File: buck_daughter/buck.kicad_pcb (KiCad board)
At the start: 2 copper layers, 35.6 x 15.2 mm, 21 parts, among them P1 Modular Jack In, U1 LD1117, U2 AP73333, U3 ST485E, U4 TPS54360DDAR

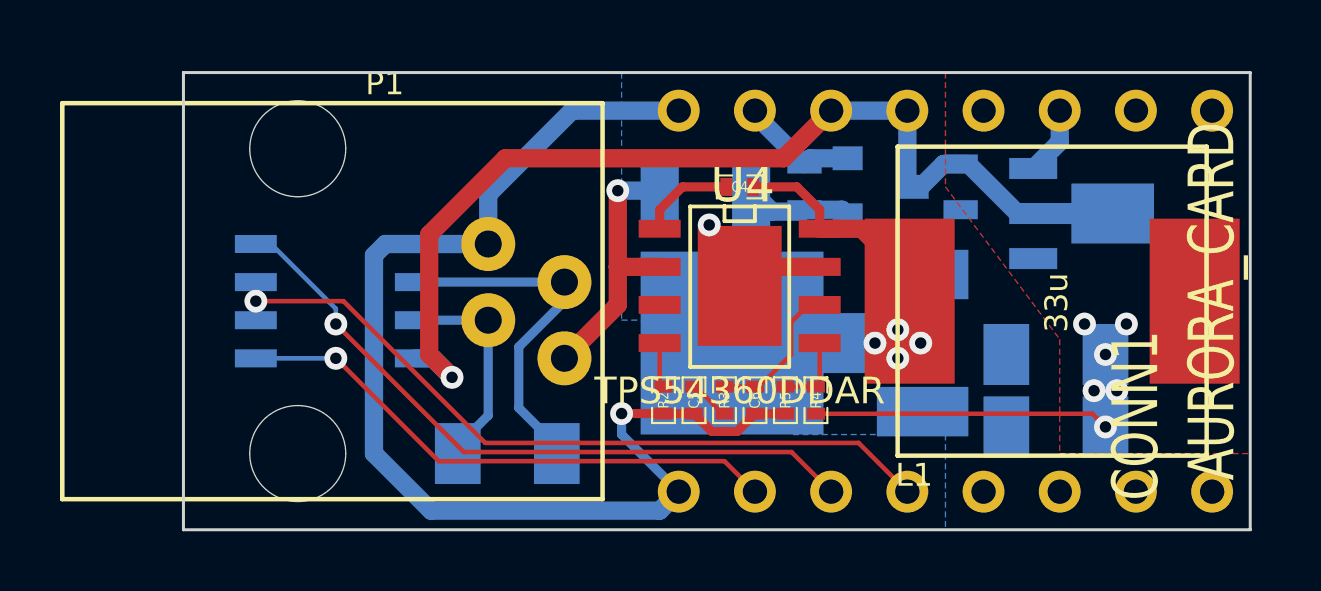
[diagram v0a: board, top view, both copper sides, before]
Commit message: Finished silkscreen on daughter board, it and digital led board are done\!
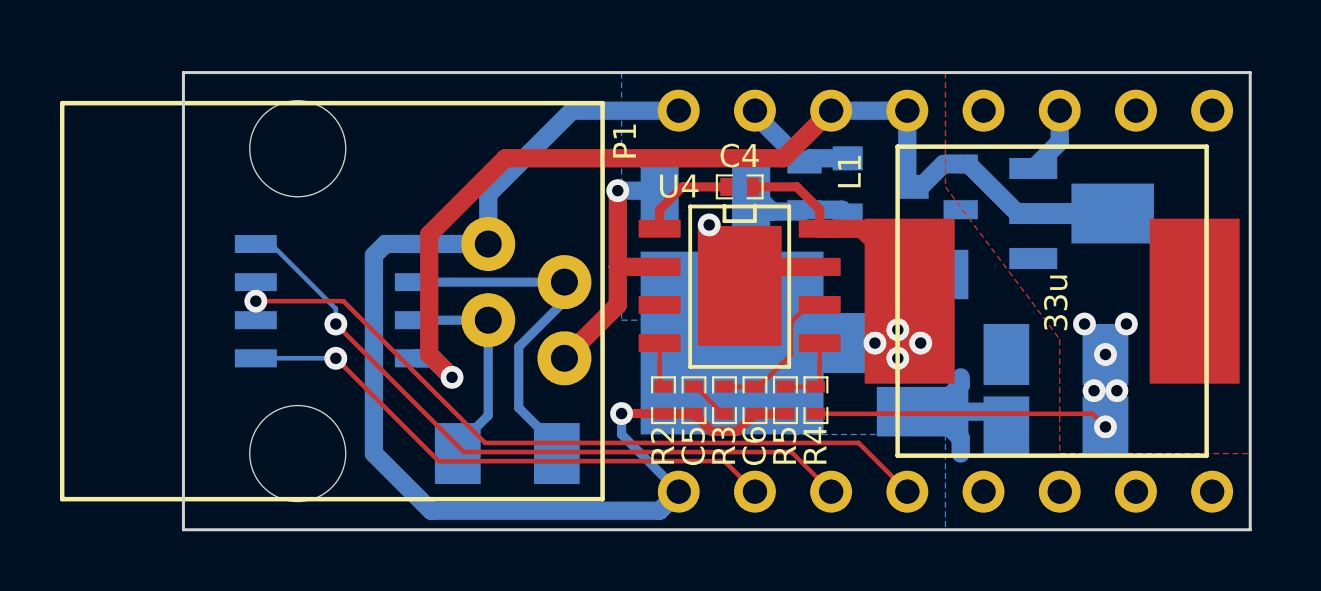
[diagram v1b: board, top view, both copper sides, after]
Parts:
- D1: value DIODE -> 50WQ10FN
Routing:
- net GND: track 49.3 -> 55.9 mm
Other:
- board text added: "Aurora Project LUX Interface"
- board text added: "rev 1"
